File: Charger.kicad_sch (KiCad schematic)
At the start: 75 parts, among them J2 Conn_02x04_Odd_Even, J4 Conn_02x05_Odd_Even, Q6 BSC0702LS, Q7 BSC0702LS, Q8 BSC0702LS, Q9 BSC0702LS, U27 BQ25756RRVR

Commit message: New conns for xESC
Added new connectors into the design for motors.
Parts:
- D2, D26: value VS-2EFH02HM3/I -> VS-2EFH02HM3/I
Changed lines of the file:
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@@
 (kicad_sch
-	(version 20231120)
+	(version 20250114)
 	(generator "eeschema")
-	(generator_version "8.0")
+	(generator_version "9.0")
 	(paper "A3")
+	(text "6S\nRBot = 16.2 kOhms gives 4.15V cell end voltage."
+		(exclude_from_sim no)
+		(at 291.338 233.172 0)
+		(effects
+			(font
+				(size 1.27 1.27)
+			)
+			(justify left)
+		)
+	)
+	(text "Custom"
+		(exclude_from_sim no)
+		(at 451.358 234.442 0)
+		(effects
+			(font
+				(size 1.27 1.27)
+			)
+			(justify left)
+		)
+	)
+	(text "7S\nRBot = 14.04 kOhms gives 4.12V cell end voltage.\n14.04 = 220k and 15k in parallel"
+		(exclude_from_sim no)
+		(at 347.218 234.442 0)
+		(effects
+			(font
+				(size 1.27 1.27)
+			)
+			(justify left)
+		)
+	)
+	(text "5S\nRBot = 20.0 kOhms gives 4.14V cell end voltage."
+		(exclude_from_sim no)
+		(at 239.268 233.172 0)
+		(effects
+			(font
+				(size 1.27 1.27)
+			)
+			(justify left)
+		)
+	)
+	(text "8S\nRBot = 12.1 kOhms gives 4.15V cell end voltage.\n"
+		(exclude_from_sim no)
+		(at 399.288 234.442 0)
+		(effects
+			(font
+				(size 1.27 1.27)
+			)
+			(justify left)
+		)
+	)
 	(junction
 		(at 336.55 132.08)
@@
 		)
 	)
-	(text "6S\nRBot = 16.2 kOhms gives 4.15V cell end voltage."
-		(exclude_from_sim no)
-		(at 291.338 233.172 0)
-		(effects
-			(font
-				(size 1.27 1.27)
-			)
-			(justify left)
-		)
-	)
-	(text "Custom"
-		(exclude_from_sim no)
-		(at 451.358 234.442 0)
-		(effects
-			(font
-				(size 1.27 1.27)
-			)
-			(justify left)
-		)
-	)
-	(text "7S\nRBot = 14.04 kOhms gives 4.12V cell end voltage.\n14.04 = 220k and 15k in parallel"
-		(exclude_from_sim no)
-		(at 347.218 234.442 0)
-		(effects
-			(font
-				(size 1.27 1.27)
-			)
-			(justify left)
-		)
-	)
-	(text "5S\nRBot = 20.0 kOhms gives 4.14V cell end voltage."
-		(exclude_from_sim no)
-		(at 239.268 233.172 0)
-		(effects
-			(font
-				(size 1.27 1.27)
-			)
-			(justify left)
-		)
-	)
-	(text "8S\nRBot = 12.1 kOhms gives 4.15V cell end voltage.\n"
-		(exclude_from_sim no)
-		(at 399.288 234.442 0)
-		(effects
-			(font
-				(size 1.27 1.27)
-			)
-			(justify left)
-		)
-	)
 	(label "FB"
 		(at 299.72 177.8 0)
-		(fields_autoplaced yes)
 		(effects
 			(font
@@
 	(label "FBG"
 		(at 331.47 186.69 0)
-		(fields_autoplaced yes)
 		(effects
 			(font
@@
 	(label "TS"
 		(at 139.7 146.05 0)
-		(fields_autoplaced yes)
 		(effects
 			(font
@@
 	(label "REGN"
 		(at 160.02 273.05 0)
-		(fields_autoplaced yes)
 		(effects
 			(font
@@
 	(label "SRP"
 		(at 118.11 130.81 0)
-		(fields_autoplaced yes)
 		(effects
 			(font
@@
 	(label "STAT1"
 		(at 189.23 153.67 180)
-		(fields_autoplaced yes)
 		(effects
 			(font
@@
 	(label "REGN"
 		(at 194.31 143.51 180)
-		(fields_autoplaced yes)
 		(effects
 			(font
@@
 	(label "FB"
 		(at 139.7 140.97 180)
-		(fields_autoplaced yes)
 		(effects
 			(font
@@
 	(label "FBG"
 		(at 452.12 227.33 0)
-		(fields_autoplaced yes)
 		(effects
 			(font
@@
 	(label "SRP"
 		(at 372.11 161.29 0)
-		(fields_autoplaced yes)
 		(effects
 			(font
@@
 	(label "DRV_SUP"
 		(at 194.31 118.11 0)
-		(fields_autoplaced yes)
 		(effects
 			(font
@@
 	(label "TS"
 		(at 199.39 257.81 0)
-		(fields_autoplaced yes)
 		(effects
 			(font
@@
 	(label "5V"
 		(at 237.49 248.92 0)
-		(fields_autoplaced yes)
 		(effects
 			(font
@@
 	(label "FBG"
 		(at 292.1 226.06 0)
-		(fields_autoplaced yes)
 		(effects
 			(font
@@
 	(label "I2C.SDA"
 		(at 185.42 168.91 0)
-		(fields_autoplaced yes)
 		(effects
 			(font
@@
 	(label "SRN"
 		(at 118.11 133.35 0)
-		(fields_autoplaced yes)
 		(effects
 			(font
@@
 	(label "STAT2"
 		(at 189.23 156.21 180)
-		(fields_autoplaced yes)
 		(effects
 			(font
@@
 	(label "~{PG}"
 		(at 252.73 266.7 270)
-		(fields_autoplaced yes)
 		(effects
 			(font
@@
 	(label "STAT2"
 		(at 245.11 266.7 270)
-		(fields_autoplaced yes)
 		(effects
 			(font
@@
 	(label "ICHG"
 		(at 138.43 151.13 0)
-		(fields_autoplaced yes)
 		(effects
 			(font
@@
 	(label "5V"
 		(at 43.18 19.05 180)
-		(fields_autoplaced yes)
 		(effects
 			(font
@@
 	(label "FB"
 		(at 331.47 179.07 0)
-		(fields_autoplaced yes)
 		(effects
 			(font
@@
 	(label "ICHG"
 		(at 102.87 189.23 0)
-		(fields_autoplaced yes)
 		(effects
 			(font
@@
 	(label "~{PG}"
 		(at 189.23 161.29 180)
-		(fields_autoplaced yes)
 		(effects
 			(font
@@
 	(label "FB"
 		(at 422.91 138.43 0)
-		(fields_autoplaced yes)
 		(effects
 			(font
@@
 	(label "STAT1"
 		(at 237.49 266.7 270)
-		(fields_autoplaced yes)
 		(effects
 			(font
@@
 	(label "FBG"
 		(at 347.98 227.33 0)
-		(fields_autoplaced yes)
 		(effects
 			(font
@@
 	(label "FBG"
 		(at 400.05 227.33 0)
-		(fields_autoplaced yes)
 		(effects
 			(font
@@
 	(label "I2C.SCL"
 		(at 185.42 166.37 0)
-		(fields_autoplaced yes)
 		(effects
 			(font
@@
 	(label "DRV_SUP"
 		(at 163.83 267.97 0)
-		(fields_autoplaced yes)
 		(effects
 			(font
@@
 	(label "FBG"
 		(at 414.02 144.78 0)
-		(fields_autoplaced yes)
 		(effects
 			(font
@@
 	(label "REGN"
 		(at 204.47 242.57 180)
-		(fields_autoplaced yes)
 		(effects
 			(font
@@
 	(label "FBG"
 		(at 139.7 138.43 180)
-		(fields_autoplaced yes)
 		(effects
 			(font
@@
 	(label "FBG"
 		(at 240.03 226.06 0)
-		(fields_autoplaced yes)
 		(effects
 			(font
@@
 	(label "SRN"
 		(at 401.32 161.29 0)
-		(fields_autoplaced yes)
 		(effects
 			(font
@@
 		(shape output)
 		(at 478.79 124.46 0)
-		(fields_autoplaced yes)
 		(effects
 			(font
@@
 		(shape input)
 		(at 35.56 19.05 180)
-		(fields_autoplaced yes)
 		(effects
 			(font
@@
 		(shape input)
 		(at 198.12 257.81 180)
-		(fields_autoplaced yes)
 		(effects
 			(font
@@
 		(shape input)
 		(at 46.99 262.89 180)
-		(fields_autoplaced yes)
 		(effects
 			(font
@@
 		(shape input)
 		(at 36.83 55.88 180)
-		(fields_autoplaced yes)
 		(effects
 			(font
@@
 			)
 		)
-		(property "Value" "    VS-2EFH02HM3/I"
+		(property "Value" "VS-2EFH02HM3/I"
 			(at 200.66 95.5674 90)
 			(effects
@@
 			)
 		)
-		(property "Value" "    VS-2EFH02HM3/I"
+		(property "Value" "VS-2EFH02HM3/I"
 			(at 218.44 95.5674 90)
 			(effects

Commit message: Routing progress
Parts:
- U27: Description_1 Stand-alone or I&sup2;C-controlled 70-V bidirectional buck-boost charge controller with MPPT -> Stand-alone or I&sup2;C-controlled 70-V bidirectional buck-boost charge controller with MPPT
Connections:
- net REGN: no longer C84.1, U27.24 (REGN)
- new net: C84.1, U27.24 (REGN)
- now unconnected: U27.15 (NC), U27.16 (NC), U27.31 (NC)
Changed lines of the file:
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@@
 	)
 	(junction
+		(at 187.96 175.26)
+		(diameter 0)
+		(color 0 0 0 0)
+	)
+	(junction
 		(at 107.95 203.2)
 		(diameter 0)
@@
 	)
 	(junction
-		(at 193.04 143.51)
+		(at 185.42 102.87)
 		(diameter 0)
 		(color 0 0 0 0)
@@
 	)
 	(junction
-		(at 194.31 118.11)
+		(at 48.26 55.88)
 		(diameter 0)
 		(color 0 0 0 0)
 	)
 	(junction
-		(at 48.26 55.88)
+		(at 386.08 139.7)
 		(diameter 0)
 		(color 0 0 0 0)
 	)
 	(junction
-		(at 386.08 139.7)
+		(at 187.96 177.8)
 		(diameter 0)
 		(color 0 0 0 0)
@@
 	)
 	(junction
-		(at 185.42 102.87)
-		(diameter 0)
-		(color 0 0 0 0)
-	)
-	(junction
 		(at 77.47 63.5)
 		(diameter 0)
@@
 	)
 	(junction
-		(at 185.42 176.53)
-		(diameter 0)
-		(color 0 0 0 0)
-	)
-	(junction
 		(at 455.93 124.46)
 		(diameter 0)
@@
 	)
 	(junction
+		(at 194.31 119.38)
+		(diameter 0)
+		(color 0 0 0 0)
+	)
+	(junction
 		(at 347.98 209.55)
 		(diameter 0)
@@
 	)
 	(junction
+		(at 187.96 109.22)
+		(diameter 0)
+		(color 0 0 0 0)
+	)
+	(junction
 		(at 321.31 124.46)
 		(diameter 0)
@@
 	(wire
 		(pts
+			(xy 185.42 177.8) (xy 187.96 177.8)
+		)
+		(stroke
+			(width 0)
+			(type default)
+		)
+	)
+	(wire
+		(pts
 			(xy 240.03 195.58) (xy 297.18 195.58)
 		)
@@
 	(wire
 		(pts
+			(xy 185.42 102.87) (xy 187.96 102.87)
+		)
+		(stroke
+			(width 0)
+			(type default)
+		)
+	)
+	(wire
+		(pts
 			(xy 100.33 217.17) (xy 88.9 217.17)
 		)
@@
 	(wire
 		(pts
+			(xy 185.42 114.3) (xy 198.12 114.3)
+		)
+		(stroke
+			(width 0)
+			(type default)
+		)
+	)
+	(wire
+		(pts
 			(xy 365.76 209.55) (xy 347.98 209.55)
 		)
@@
 	(wire
 		(pts
+			(xy 185.42 116.84) (xy 215.9 116.84)
+		)
+		(stroke
+			(width 0)
+			(type default)
+		)
+	)
+	(wire
+		(pts
 			(xy 105.41 215.9) (xy 105.41 220.98)
 		)
@@
 	(wire
 		(pts
+			(xy 187.96 180.34) (xy 187.96 177.8)
+		)
+		(stroke
+			(width 0)
+			(type default)
+		)
+	)
+	(wire
+		(pts
 			(xy 422.91 133.35) (xy 422.91 138.43)
 		)
@@
 	(wire
 		(pts
+			(xy 194.31 119.38) (xy 203.2 119.38)
+		)
+		(stroke
+			(width 0)
+			(type default)
+		)
+	)
+	(wire
+		(pts
 			(xy 238.76 137.16) (xy 238.76 139.7)
 		)
@@
 	(wire
 		(pts
+			(xy 198.12 106.68) (xy 198.12 114.3)
+		)
+		(stroke
+			(width 0)
+			(type default)
+		)
+	)
+	(wire
+		(pts
 			(xy 224.79 106.68) (xy 198.12 106.68)
 		)
@@
 	(wire
 		(pts
+			(xy 185.42 111.76) (xy 187.96 111.76)
+		)
+		(stroke
+			(width 0)
+			(type default)
+		)
+	)
+	(wire
+		(pts
 			(xy 88.9 228.6) (xy 100.33 228.6)
 		)
@@
 	(wire
 		(pts
-			(xy 185.42 110.49) (xy 185.42 102.87)
-		)
-		(stroke
-			(width 0)
-			(type default)
-		)
-	)
-	(wire
-		(pts
 			(xy 204.47 273.05) (xy 204.47 270.51)
 		)
@@
 	(wire
 		(pts
-			(xy 194.31 118.11) (xy 205.74 118.11)
-		)
-		(stroke
-			(width 0)
-			(type default)
-		)
-	)
-	(wire
-		(pts
 			(xy 312.42 186.69) (xy 312.42 193.04)
 		)
@@
 	(wire
 		(pts
-			(xy 185.42 176.53) (xy 185.42 184.15)
+			(xy 185.42 172.72) (xy 187.96 172.72)
 		)
 		(stroke
@@
 	(wire
 		(pts
-			(xy 198.12 113.03) (xy 185.42 113.03)
-		)
-		(stroke
-			(width 0)
-			(type default)
-		)
-	)
-	(wire
-		(pts
 			(xy 185.42 102.87) (xy 185.42 100.33)
 		)
@@
 	(wire
 		(pts
-			(xy 237.49 248.92) (xy 245.11 248.92)
+			(xy 187.96 109.22) (xy 187.96 102.87)
 		)
 		(stroke
@@
 	(wire
 		(pts
-			(xy 109.22 73.66) (xy 109.22 55.88)
+			(xy 237.49 248.92) (xy 245.11 248.92)
 		)
 		(stroke
@@
 	(wire
 		(pts
-			(xy 133.35 219.71) (xy 133.35 220.98)
+			(xy 109.22 73.66) (xy 109.22 55.88)
 		)
 		(stroke
@@
 	(wire
 		(pts
-			(xy 144.78 123.19) (xy 144.78 125.73)
+			(xy 133.35 219.71) (xy 133.35 220.98)
 		)
 		(stroke
@@
 	(wire
 		(pts
-			(xy 257.81 208.28) (xy 240.03 208.28)
+			(xy 144.78 123.19) (xy 144.78 125.73)
 		)
 		(stroke
@@
 	(wire
 		(pts
-			(xy 194.31 118.11) (xy 194.31 76.2)
+			(xy 257.81 208.28) (xy 240.03 208.28)
 		)
 		(stroke
@@
 	(wire
 		(pts
-			(xy 198.12 106.68) (xy 198.12 113.03)
+			(xy 194.31 119.38) (xy 194.31 76.2)
 		)
 		(stroke
@@
 	(wire
 		(pts
+			(xy 187.96 175.26) (xy 187.96 177.8)
+		)
+		(stroke
+			(width 0)
+			(type default)
+		)
+	)
+	(wire
+		(pts
 			(xy 372.11 124.46) (xy 382.27 124.46)
 		)
@@
 	(wire
 		(pts
-			(xy 281.94 137.16) (xy 281.94 139.7)
+			(xy 187.96 172.72) (xy 187.96 175.26)
 		)
 		(stroke
@@
 	(wire
 		(pts
-			(xy 185.42 100.33) (xy 175.26 100.33)
+			(xy 281.94 137.16) (xy 281.94 139.7)
 		)
 		(stroke
@@
 	(wire
 		(pts
-			(xy 398.78 139.7) (xy 401.32 139.7)
+			(xy 185.42 100.33) (xy 175.26 100.33)
 		)
 		(stroke
@@
 	(wire
 		(pts
-			(xy 193.04 143.51) (xy 194.31 143.51)
+			(xy 398.78 139.7) (xy 401.32 139.7)
 		)
 		(stroke
@@
 	(wire
 		(pts
-			(xy 185.42 173.99) (xy 185.42 176.53)
+			(xy 185.42 175.26) (xy 187.96 175.26)
 		)
 		(stroke
@@
 	(wire
 		(pts
-			(xy 185.42 115.57) (xy 215.9 115.57)
-		)
-		(stroke
-			(width 0)
-			(type default)
-		)
-	)
-	(wire
-		(pts
 			(xy 400.05 209.55) (xy 400.05 212.09)
 		)
@@
 	(wire
 		(pts
-			(xy 185.42 118.11) (xy 194.31 118.11)
+			(xy 185.42 119.38) (xy 194.31 119.38)
 		)
 		(stroke
@@
 	(wire
 		(pts
-			(xy 215.9 115.57) (xy 215.9 102.87)
-		)
-		(stroke
-			(width 0)
-			(type default)
-		)
-	)
-	(wire
-		(pts
 			(xy 185.42 128.27) (xy 212.09 128.27)
 		)
@@
 	(wire
 		(pts
+			(xy 187.96 111.76) (xy 187.96 109.22)
+		)
+		(stroke
+			(width 0)
+			(type default)
+		)
+	)
+	(wire
+		(pts
 			(xy 414.02 140.97) (xy 414.02 144.78)
 		)
@@
 	(wire
 		(pts
+			(xy 185.42 109.22) (xy 187.96 109.22)
+		)
+		(stroke
+			(width 0)
+			(type default)
+		)
+	)
+	(wire
+		(pts
 			(xy 105.41 203.2) (xy 107.95 203.2)
 		)
@@
 	(wire
 		(pts
+			(xy 215.9 102.87) (xy 215.9 116.84)
+		)
+		(stroke
+			(width 0)
+			(type default)
+		)
+	)
+	(wire
+		(pts
 			(xy 107.95 203.2) (xy 110.49 203.2)
 		)
@@
 	)
 	(label "DRV_SUP"
-		(at 194.31 118.11 0)
+		(at 203.2 119.38 180)
 		(effects
 			(font
 				(size 1.27 1.27)
 			)
-			(justify left bottom)
+			(justify right bottom)
 		)
 	)
@@
 			)
 		)
-		(property "Description_1" "\nStand-alone or I&sup2;C-controlled 70-V bidirectional buck-boost charge controller with MPPT\n"
+		(property "Description_1" "Stand-alone or I&sup2;C-controlled 70-V bidirectional buck-boost charge controller with MPPT"
 			(at 165.1 143.51 0)
 			(effects
@@
 	(symbol
 		(lib_id "power:GND")
-		(at 185.42 184.15 0)
+		(at 187.96 180.34 0)
 		(unit 1)
 		(exclude_from_sim no)
@@
 		(fields_autoplaced yes)
 		(property "Reference" "#PWR0144"
-			(at 185.42 190.5 0)
+			(at 187.96 186.69 0)
 			(effects
 				(font
@@
 		)
 		(property "Value" "GND"
-			(at 185.42 189.23 0)
+			(at 187.96 185.42 0)
 			(effects
 				(font
@@
 		)
 		(property "Footprint" ""
-			(at 185.42 184.15 0)
+			(at 187.96 180.34 0)
 			(effects
 				(font
@@
 		)
 		(property "Datasheet" ""
-			(at 185.42 184.15 0)
+			(at 187.96 180.34 0)
 			(effects
 				(font
@@
 		)
 		(property "Description" "Power symbol creates a global label with name \"GND\" , ground"
-			(at 185.42 184.15 0)
+			(at 187.96 180.34 0)
 			(effects
 				(font

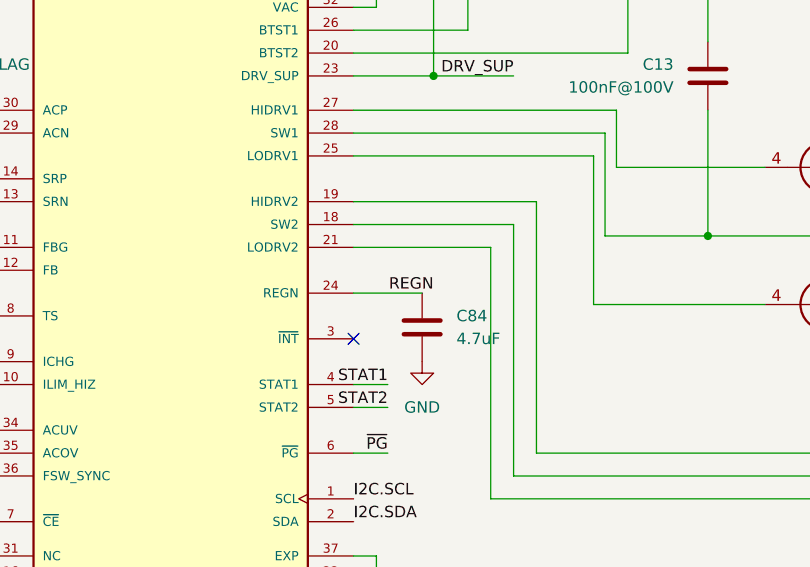
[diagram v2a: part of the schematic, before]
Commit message: Review ready layout
DRC mostly clean.  Need to add GND via stitching and GND return vias yet, and general review
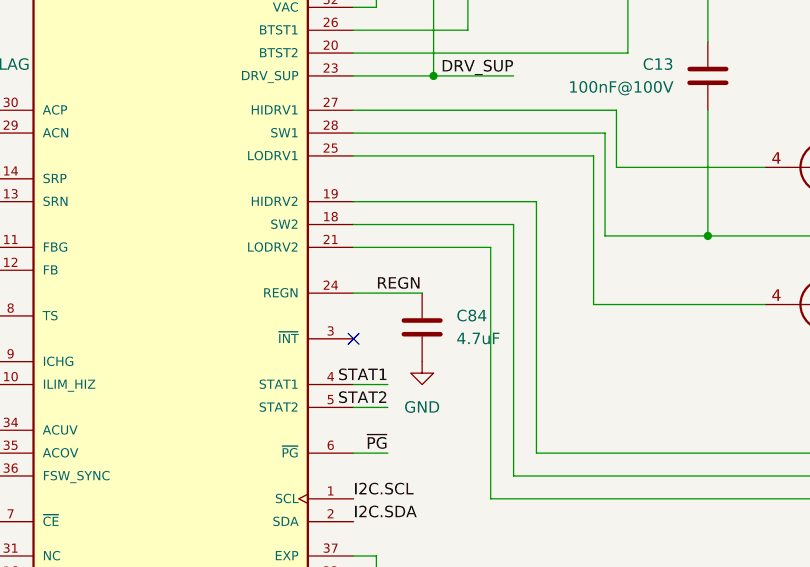
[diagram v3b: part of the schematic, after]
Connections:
- net REGN: now also C84.1, U27.24 (REGN)
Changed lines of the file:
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@@
 	)
 	(label "REGN"
-		(at 194.31 143.51 180)
+		(at 187.96 143.51 0)
 		(effects
 			(font
 				(size 1.27 1.27)
 			)
-			(justify right bottom)
+			(justify left bottom)
 		)
 	)
